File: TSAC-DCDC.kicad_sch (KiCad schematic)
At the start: 28 parts, among them J1 HVCONN, J2 LVCONN, Q1 NMOS, T1 Transformer_1P_2S, U1 UCC28C44DR, U2 Opto, U3 TL432DBZ

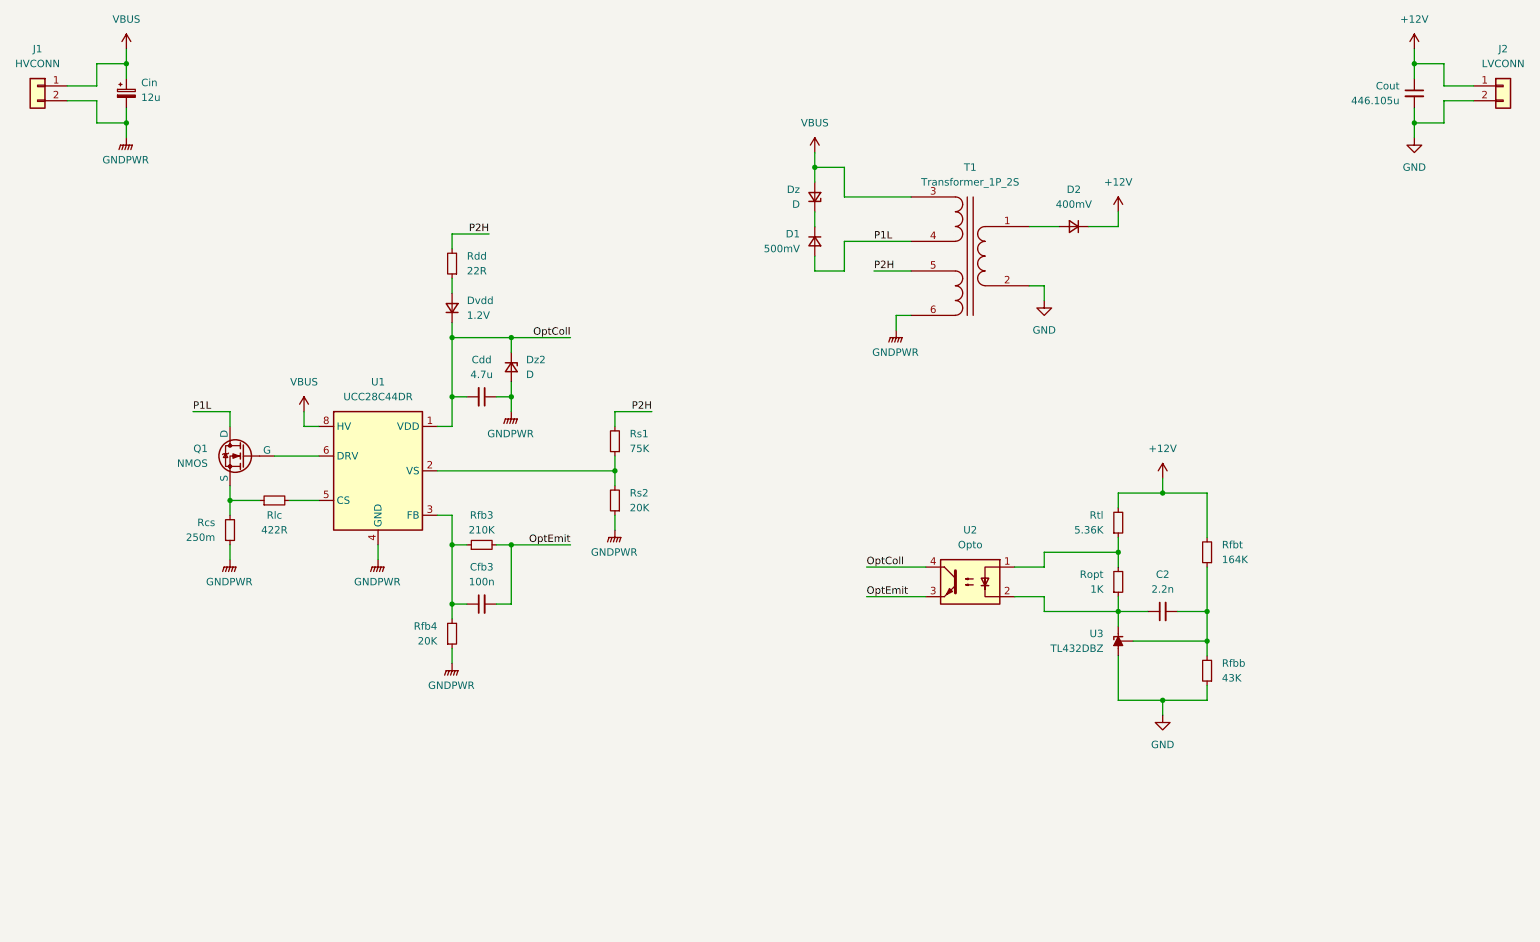
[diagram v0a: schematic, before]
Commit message: Rearrange sch for cleaner look.
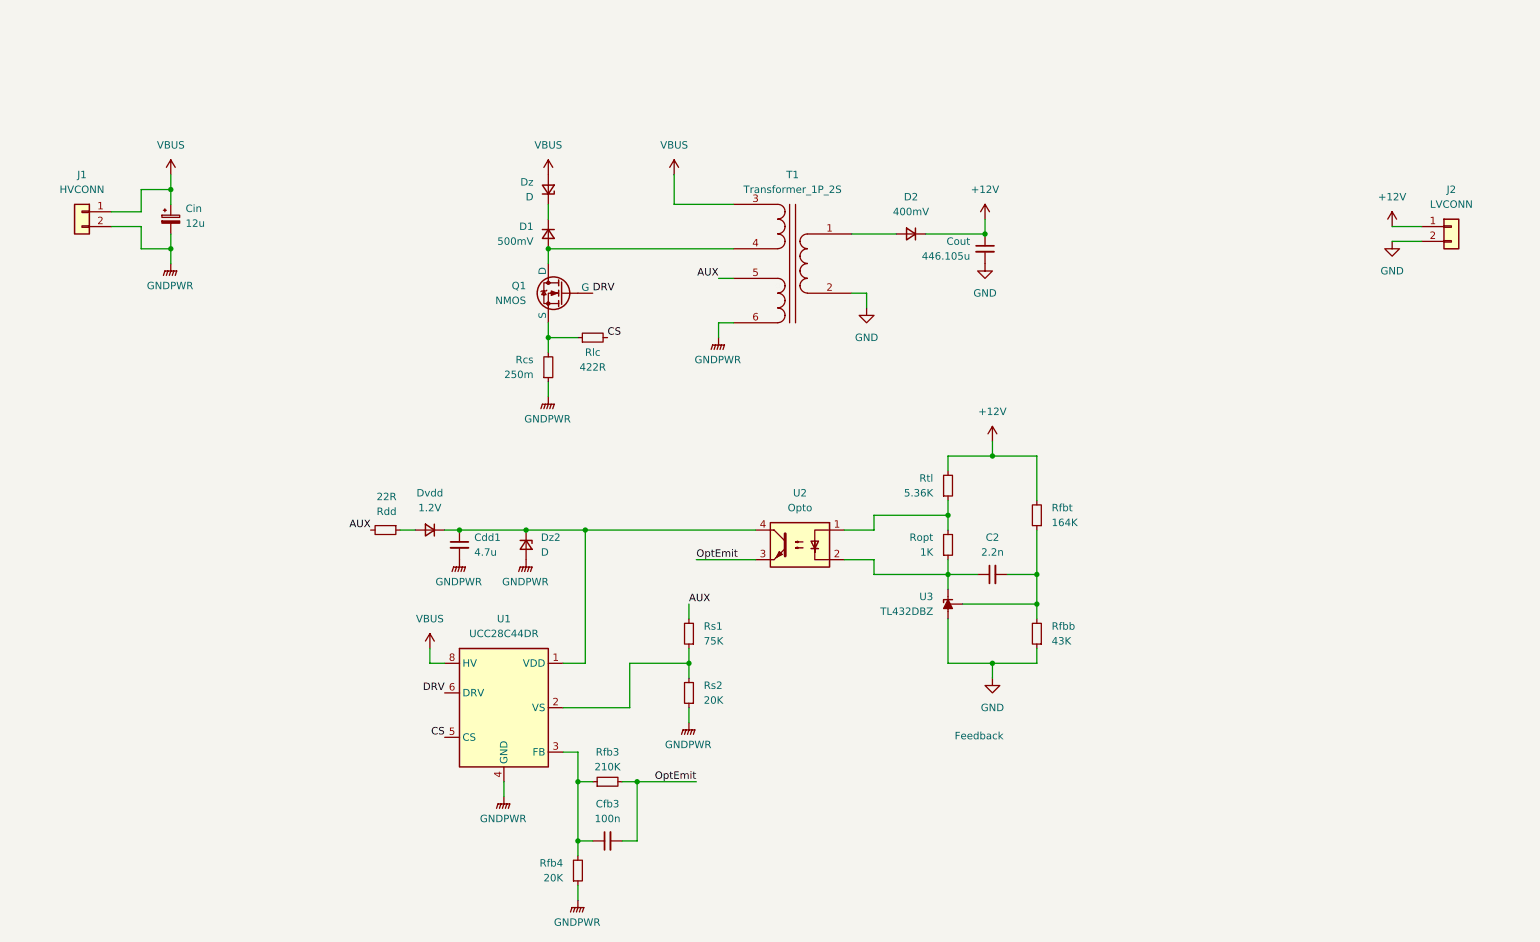
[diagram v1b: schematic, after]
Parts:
- removed Cdd: 4.7u, symbol Device:C_Small
- added Cdd1: 4.7u, symbol Device:C_Small
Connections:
- net GNDPWR: now also Cdd1.2
- net DRV: now reaches Q1.2 (G), U1.6 (DRV)
- net CS: now reaches Rlc.2, U1.5 (CS)
- net OptColl: no longer names the net of Dvdd.1 (K), Dz2.1 (K), U1.1 (VDD), U2.4
- net OptColl: now also Cdd1.1
- net P1L: no longer names the net of D1.2 (A), Q1.1 (D), T1.4 (SB)
- net P2H renamed AUX
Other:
- note added: "Feedback"
- moved on the sheet: C2, Cfb3, Cin, Cout, D1, D2, Dvdd, Dz, Dz2, J1, J2, Q1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

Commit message: transformer pin update
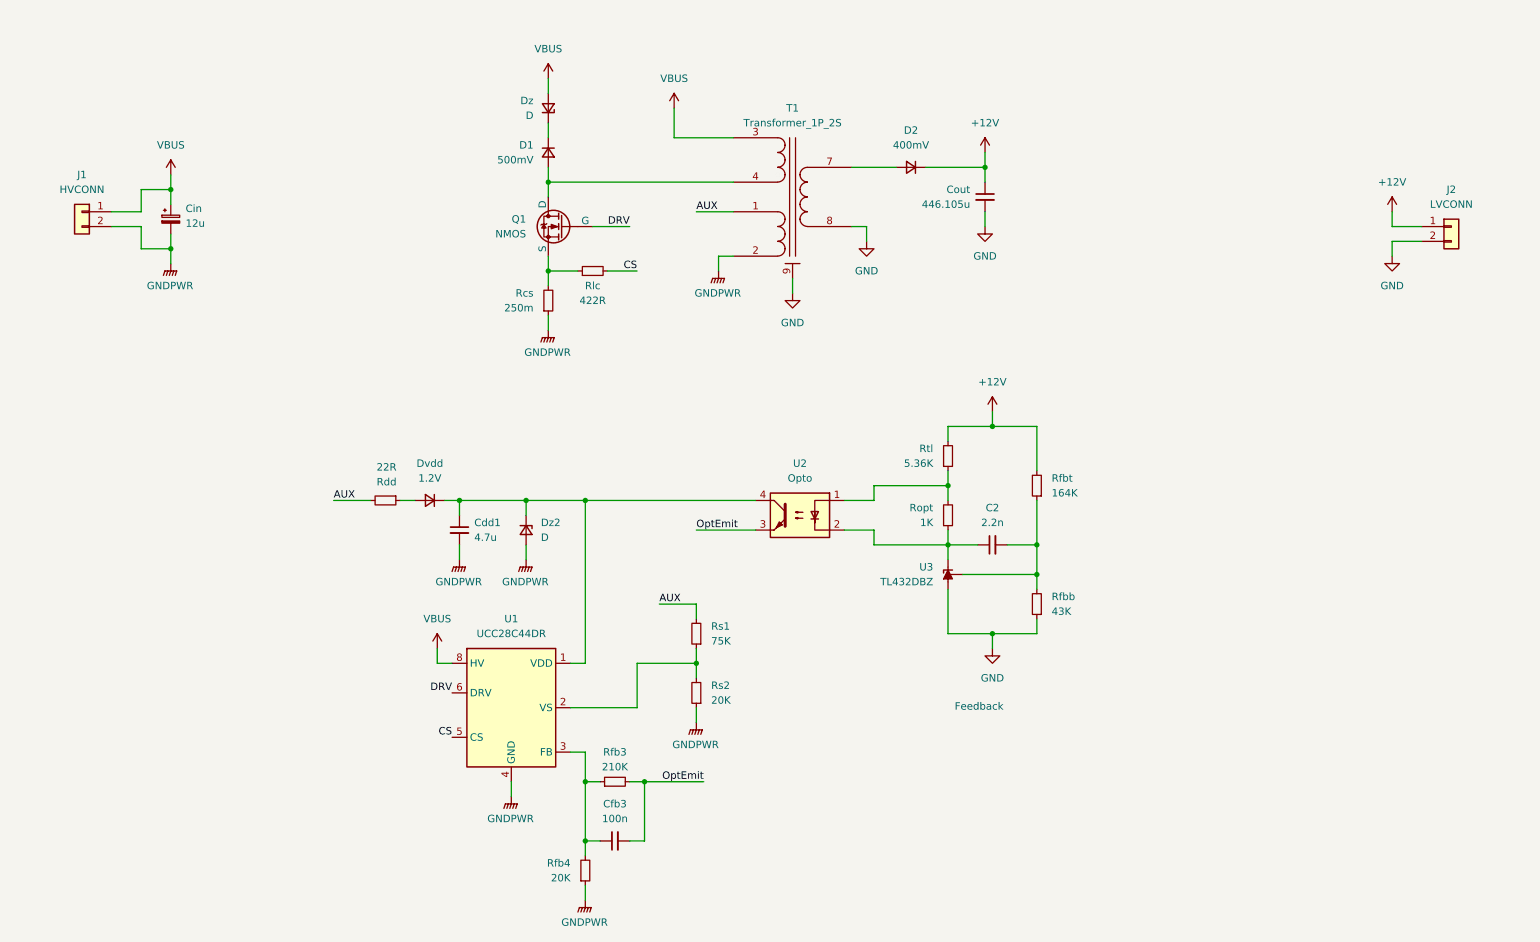
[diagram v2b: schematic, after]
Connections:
- net AUX: now also T1.1 (SC); no longer T1.5 (SC)
- net GND: now also T1.8 (AB), T1.9 (MH); no longer T1.2 (AB)
- net GNDPWR: now also T1.2 (SD); no longer T1.6 (SD)
- net at D2.2 (A): now also T1.7 (AA); no longer T1.1 (AA)
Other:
- moved on the sheet: C2, Cdd1, Cfb3, Cout, D1, D2, Dvdd, Dz, Dz2, Q1, Rcs, Rdd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

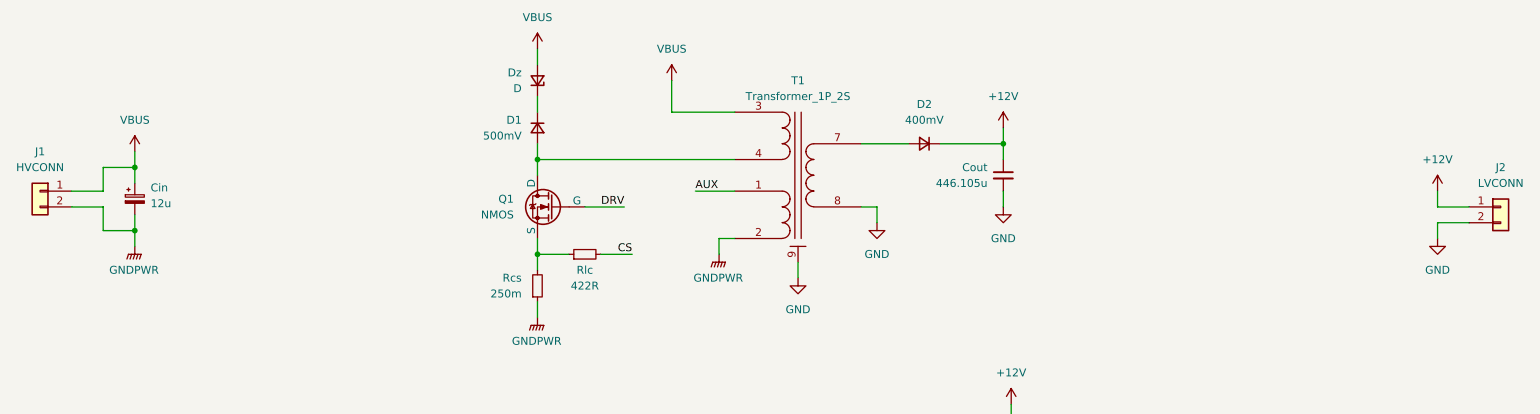
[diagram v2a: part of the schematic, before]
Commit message: Add fuse to power input and output
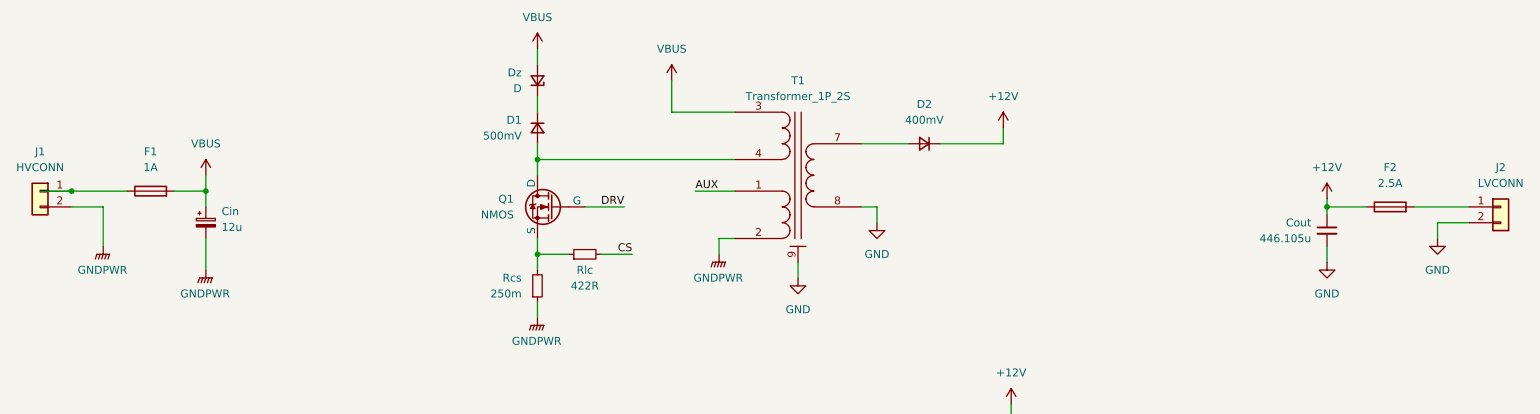
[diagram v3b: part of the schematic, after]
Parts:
- added F1: 1A, symbol Device:Fuse
- added F2: 2.5A, symbol Device:Fuse
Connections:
- net +12V: now also F2.1; no longer J2.1 (Pin_1)
- net VBUS: now also F1.2; no longer J1.1 (Pin_1)
- new net: F1.1, J1.1 (Pin_1)
- new net: F2.2, J2.1 (Pin_1)
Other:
- moved on the sheet: Cin, Cout

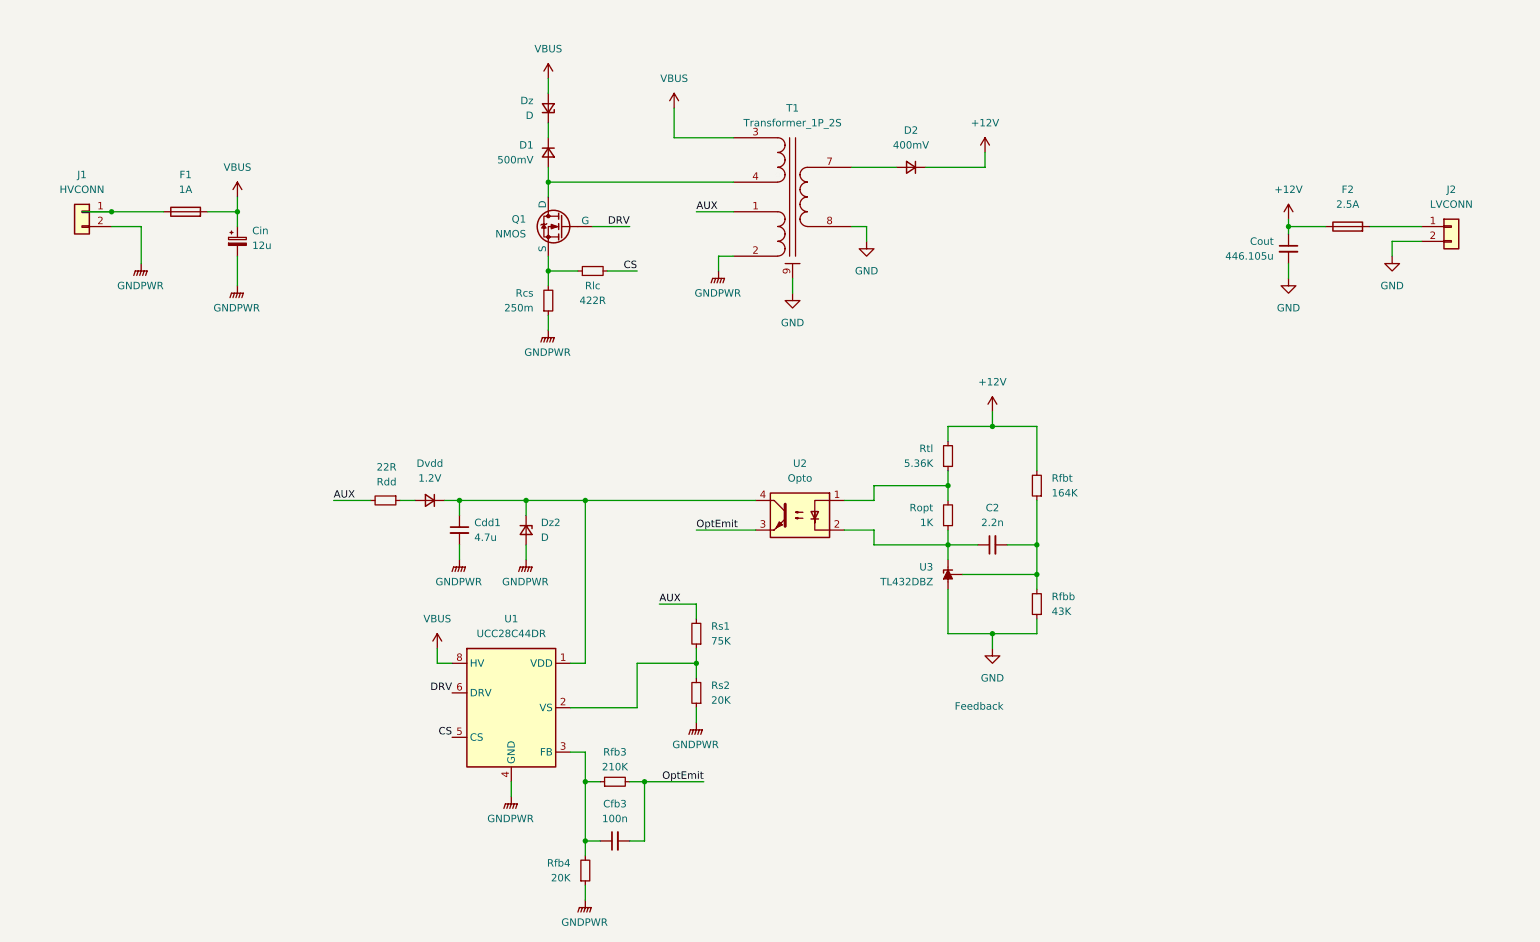
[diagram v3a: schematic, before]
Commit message: Add footprint to components
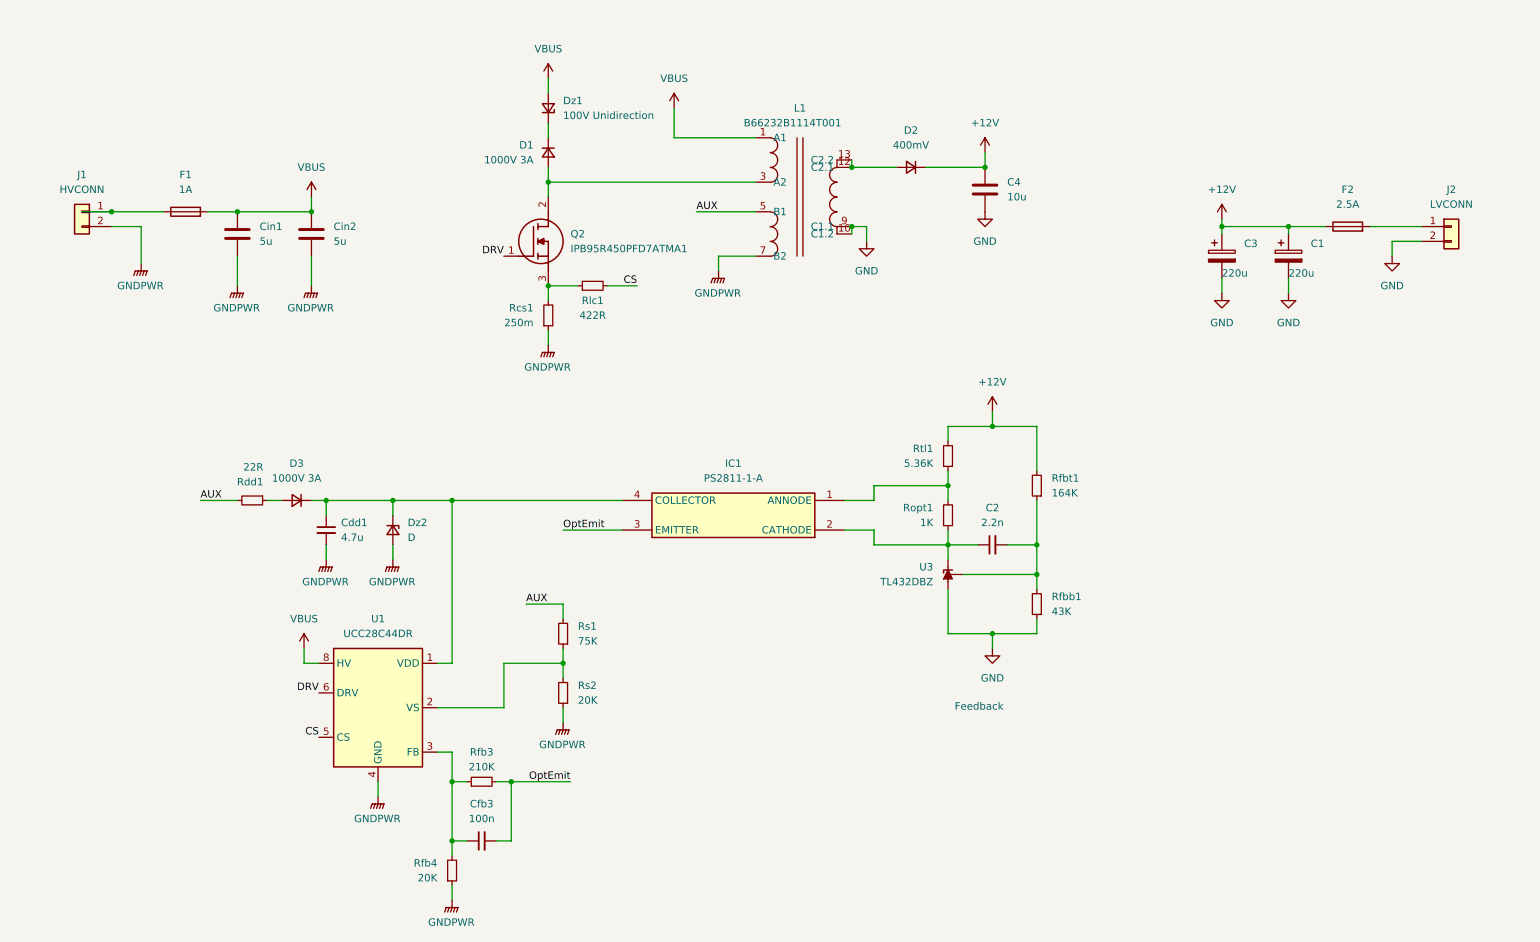
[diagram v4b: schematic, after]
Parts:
- removed Cout: 446.105u, symbol Device:C_Small
- removed Dvdd: 1.2V, symbol Device:D_Small
- removed Q1: NMOS, symbol Simulation_SPICE:NMOS
- removed T1: Transformer_1P_2S, symbol customSymbols:Transformer_1P_2S
- removed U2: Opto, symbol Isolator:Optocoupler_DC_PhotoNPN_AKEC
- added C1, C3: 220u, Capacitor_THT:CP_Radial_D8.0mm_P3.50mm, symbol Device:C_Polarized
- added C4: 10u, Capacitor_SMD:C_0603_1608Metric, symbol Device:C
- added Cin2: 5u, Samacsys:ECWFG60505JA, symbol Device:C
- added D3: 1000V 3A, Diode_SMD:D_SMB, symbol Device:D_Small
- added IC1: PS2811-1-A, Samacsys:SOIC127P700X210-4N, symbol Samacsys:PS2811-1-A
- added L1: B66232B1114T001, Samacsys:B66232B1114T001, symbol Samacsys:B66232B1114T001
- added Q2: IPB95R450PFD7ATMA1, Samacsys:IPB95R450PFD7ATMA1, symbol Samacsys:IPB95R450PFD7ATMA1
- C2, Cdd1, Cfb3: footprint (none) -> Capacitor_SMD:C_0603_1608Metric
- Cin1: renamed from Cin; value 12u -> 5u; footprint (none) -> Samacsys:ECWFG60505JA; symbol Device:C_Polarized_Small -> Device:C
- D1: value 500mV -> 1000V 3A; footprint (none) -> Diode_SMD:D_SMB
- D2: footprint (none) -> Diode_SMD:D_SMC
- Dz1: renamed from Dz; value D -> 100V Unidirection; footprint (none) -> Diode_SMD:D_SMC
- F1, F2: footprint (none) -> Samacsys:FUSC13250X555N
- Rcs1: renamed from Rcs; footprint (none) -> Resistor_SMD:R_0603_1608Metric
- Rdd1: renamed from Rdd; footprint (none) -> Resistor_SMD:R_0603_1608Metric
- Rfb3, Rfb4, Rs1, Rs2: footprint (none) -> Resistor_SMD:R_0603_1608Metric
- Rfbb1: renamed from Rfbb; footprint (none) -> Resistor_SMD:R_0603_1608Metric
- Rfbt1: renamed from Rfbt; footprint (none) -> Resistor_SMD:R_0603_1608Metric
- Rlc1: renamed from Rlc; footprint (none) -> Resistor_SMD:R_0603_1608Metric
- Ropt1: renamed from Ropt; footprint (none) -> Resistor_SMD:R_0603_1608Metric
- Rtl1: renamed from Rtl; footprint (none) -> Resistor_SMD:R_0603_1608Metric
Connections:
- net +12V: now also C1.1, C3.1, C4.1
- net AUX: now also L1.5 (B1)
- net DRV: now also Q2.1 (G)
- net GND: now also C1.2, C3.2, C4.2, L1.10 (C1.2), L1.9 (C1.1)
- net GNDPWR: now also Cin2.2, L1.7 (B2)
- net OptEmit: now also IC1.3 (EMITTER)
- net VBUS: now also Cin2.1, L1.1 (A1)
- net at D1.2 (A): now also L1.3 (A2), Q2.2 (D)
- net at Rcs1.2, Rlc1.1: now also Q2.3 (S)
- net at Ropt1.2, Rtl1.1: now also IC1.1 (ANNODE)
- net at D2.2 (A): now also L1.12 (C2.1), L1.13 (C2.2)
- net at Cdd1.1, Dz2.1 (K), U1.1 (VDD): now also D3.1 (K), IC1.4 (COLLECTOR)
- net at Rdd1.1: now also D3.2 (A)
- net at C2.1, Ropt1.1, U3.2 (K): now also IC1.2 (CATHODE)
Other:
- moved on the sheet: Cdd1, Cfb3, Dz2, Rcs1, Rdd1, Rfb3, Rfb4, Rlc1, Rs1, Rs2, U1

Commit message: First try of L-C inperfection
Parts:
- D2: footprint Diode_SMD:D_SMC -> Package_TO_SOT_SMD:TO-277A
- Dz2: value D -> 24v; footprint (none) -> SOD-123-2
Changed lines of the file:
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@@
 			)
 		)
-		(property "Footprint" "Diode_SMD:D_SMC"
+		(property "Footprint" "Package_TO_SOT_SMD:TO-277A"
 			(at 170.18 44.45 90)
 			(effects
@@
 			)
 		)
-		(property "Datasheet" "https://services.taiwansemi.com/storage/resources/datasheet/SSC3H40H_A2504.pdf"
+		(property "Datasheet" "https://www.st.com/resource/en/datasheet/stpst5h100.pdf"
 			(at 170.18 44.45 90)
 			(effects
@@
 			)
 		)
-		(property "Value" "D"
+		(property "Value" "24v"
 			(at 83.82 107.9499 90)
 			(effects
@@
 			)
 		)
-		(property "Footprint" ""
+		(property "Footprint" "SOD-123-2"
 			(at 81.28 106.68 90)
 			(effects
@@
 			)
 		)
-		(property "Datasheet" "~"
+		(property "Datasheet" "https://www.mouser.co.uk/ProductDetail/onsemi/SZMMSZ4709T1G?qs=PJJcWtbOkNU8TyrVDtkUmQ%3D%3D"
 			(at 81.28 106.68 90)
 			(effects
